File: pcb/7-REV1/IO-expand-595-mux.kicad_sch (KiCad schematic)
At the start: 58 parts, among them Q2 2N7002KT, U10 LM358_DFN, U11 LM358_DFN, U12 LM358_DFN, U13 LM358_DFN, U2 74LVC8T245BQ, U402 CD4067, U503 74HCT245BQ, U9 LM358_DFN

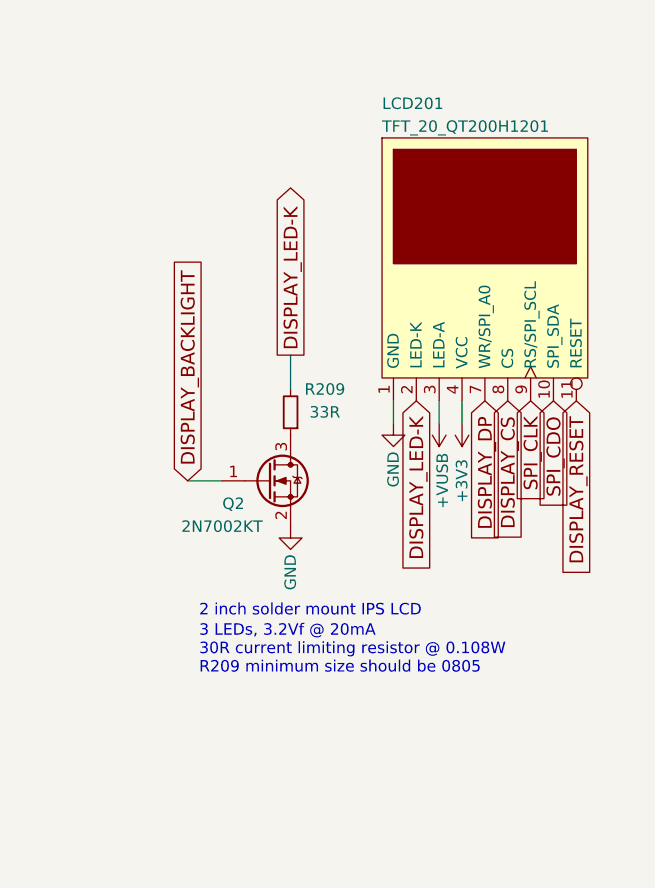
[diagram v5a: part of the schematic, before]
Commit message: move LCD background LED current limiting resistor from cathode to anode
- there were several soldering defects on the LCD connector observed during manufacturing
- often the LEDs were shorted to ground
- this modification will protect the LEDs and the traces in this case, making rework easier
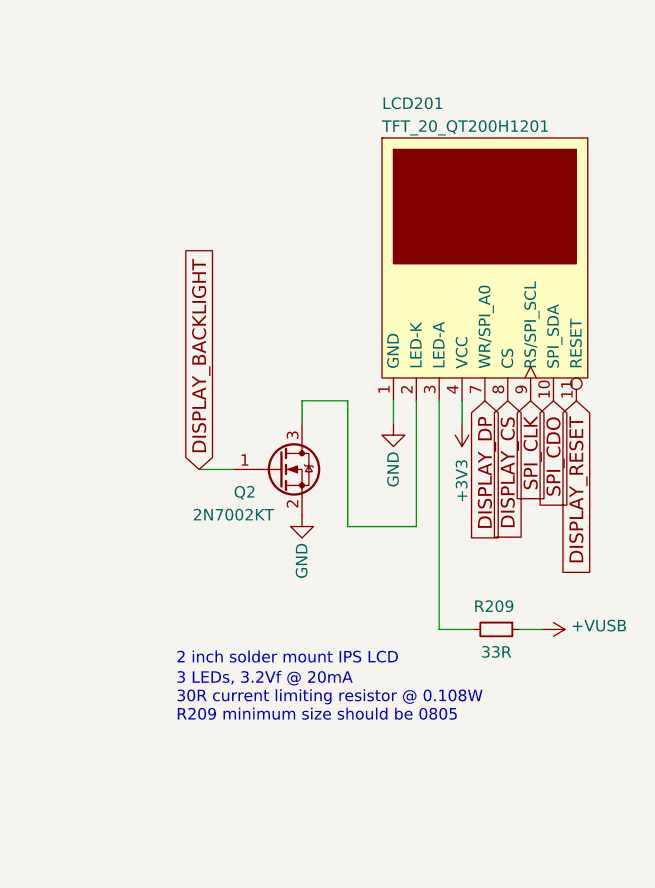
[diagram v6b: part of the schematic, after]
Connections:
- net +VUSB: now also R209.1; no longer LCD201.3 (LED-A)
- net at Q2.3 (D): now also LCD201.2 (LED-K); no longer R209.1
- net DISPLAY_LED-K: no longer names the net of R209.2
- net DISPLAY_LED-K: now also LCD201.3 (LED-A); no longer LCD201.2 (LED-K)
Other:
- moved on the sheet: Q2, R209
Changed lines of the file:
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@@
 	(wire
 		(pts
+			(xy 347.98 60.96) (xy 347.98 63.5)
+		)
+		(stroke
+			(width 0)
+			(type default)
+		)
+	)
+	(wire
+		(pts
 			(xy 157.48 121.92) (xy 157.48 115.57)
 		)
@@
 	(wire
 		(pts
+			(xy 360.68 60.96) (xy 360.68 74.93)
+		)
+		(stroke
+			(width 0)
+			(type default)
+		)
+	)
+	(wire
+		(pts
 			(xy 31.75 172.72) (xy 34.29 172.72)
 		)
@@
 	(wire
 		(pts
+			(xy 353.06 74.93) (xy 353.06 60.96)
+		)
+		(stroke
+			(width 0)
+			(type default)
+		)
+	)
+	(wire
+		(pts
 			(xy 240.03 139.7) (xy 237.49 139.7)
 		)
@@
 	(wire
 		(pts
+			(xy 372.11 86.36) (xy 374.65 86.36)
+		)
+		(stroke
+			(width 0)
+			(type default)
+		)
+	)
+	(wire
+		(pts
 			(xy 113.03 175.26) (xy 115.57 175.26)
 		)
@@
 	(wire
 		(pts
+			(xy 353.06 60.96) (xy 347.98 60.96)
+		)
+		(stroke
+			(width 0)
+			(type default)
+		)
+	)
+	(wire
+		(pts
 			(xy 260.35 125.73) (xy 260.35 128.27)
 		)
@@
 	(wire
 		(pts
+			(xy 360.68 74.93) (xy 353.06 74.93)
+		)
+		(stroke
+			(width 0)
+			(type default)
+		)
+	)
+	(wire
+		(pts
 			(xy 59.69 177.8) (xy 60.96 177.8)
 		)
@@
 	(wire
 		(pts
-			(xy 335.28 69.85) (xy 339.09 69.85)
+			(xy 336.55 68.58) (xy 340.36 68.58)
 		)
 		(stroke
@@
 	(wire
 		(pts
-			(xy 346.71 55.88) (xy 346.71 59.69)
-		)
-		(stroke
-			(width 0)
-			(type default)
-		)
-	)
-	(wire
-		(pts
 			(xy 48.26 223.52) (xy 50.8 223.52)
 		)
@@
 	(wire
 		(pts
-			(xy 363.22 60.96) (xy 363.22 63.5)
+			(xy 363.22 60.96) (xy 363.22 86.36)
 		)
 		(stroke
@@
 	(wire
 		(pts
+			(xy 367.03 86.36) (xy 363.22 86.36)
+		)
+		(stroke
+			(width 0)
+			(type default)
+		)
+	)
+	(wire
+		(pts
 			(xy 46.99 101.6) (xy 46.99 102.87)
 		)
@@
 	(text "3 LEDs, 3.2Vf @ 20mA\n30R current limiting resistor @ 0.108W\nR209 minimum size should be 0805"
 		(exclude_from_sim no)
-		(at 336.55 91.44 0)
+		(at 334.01 96.774 0)
 		(effects
 			(font
@@
 	(text "2 inch solder mount IPS LCD"
 		(exclude_from_sim no)
-		(at 336.55 85.09 0)
+		(at 334.01 90.424 0)
 		(effects
 			(font
@@
 		)
 	)
-	(global_label "DISPLAY_LED-K"
-		(shape output)
-		(at 346.71 55.88 90)
-		(effects
-			(font
-				(size 1.524 1.524)
-			)
-			(justify left)
-		)
-		(property "Intersheetrefs" "${INTERSHEET_REFS}"
-			(at 346.71 55.88 0)
-			(effects
-				(font
-					(size 1.27 1.27)
-				)
-				(hide yes)
-			)
-		)
-	)
 	(global_label "MUX_BPIO5_TVS"
 		(shape input)
@@
 	(global_label "DISPLAY_BACKLIGHT"
 		(shape input)
-		(at 335.28 69.85 90)
+		(at 336.55 68.58 90)
 		(effects
 			(font
@@
 		)
 		(property "Intersheetrefs" "${INTERSHEET_REFS}"
-			(at 335.28 69.85 0)
+			(at 336.55 68.58 0)
 			(effects
 				(font
@@
 		)
 	)
-	(global_label "DISPLAY_LED-K"
-		(shape input)
-		(at 360.68 60.96 270)
-		(effects
-			(font
-				(size 1.524 1.524)
-			)
-			(justify right)
-		)
-		(property "Intersheetrefs" "${INTERSHEET_REFS}"
-			(at 360.68 60.96 0)
-			(effects
-				(font
-					(size 1.27 1.27)
-				)
-				(hide yes)
-			)
-		)
-	)
 	(global_label "AMUX_OUT"
 		(shape output)
@@
 	(symbol
 		(lib_id "Device:R_Small")
-		(at 346.71 62.23 180)
+		(at 369.57 86.36 270)
 		(unit 1)
 		(exclude_from_sim no)
@@
 		(dnp no)
 		(property "Reference" "R209"
-			(at 350.52 59.69 0)
+			(at 369.316 83.82 90)
 			(effects
 				(font
@@
 		)
 		(property "Value" "33R"
-			(at 350.52 62.23 0)
+			(at 369.57 88.9 90)
 			(effects
 				(font
@@
 		)
 		(property "Footprint" "Resistor_SMD:R_0805_2012Metric"
-			(at 346.71 62.23 0)
+			(at 369.57 86.36 0)
 			(effects
 				(font
@@
 		)
 		(property "Datasheet" "~"
-			(at 346.71 62.23 0)
+			(at 369.57 86.36 0)
 			(effects
 				(font
@@
 		)
 		(property "Description" ""
-			(at 346.71 62.23 0)
+			(at 369.57 86.36 0)
 			(effects
 				(font
@@
 		)
 		(property "RMB" "0.019315"
-			(at 346.71 62.23 0)
+			(at 369.57 86.36 0)
 			(effects
 				(font
@@
 		)
 		(property "Supplier" "https://item.szlcsc.com/139271.html"
-			(at 346.71 62.23 0)
+			(at 369.57 86.36 0)
 			(effects
 				(font
@@
 		)
 		(property "Description_1" ""
-			(at 346.71 62.23 0)
+			(at 369.57 86.36 0)
 			(effects
 				(font
@@
 		)
 		(property "MAXIMUM_PACKAGE_HEIGHT" ""
-			(at 346.71 62.23 0)
+			(at 369.57 86.36 0)
 			(effects
 				(font
@@
 		)
 		(property "PARTREV" ""
-			(at 346.71 62.23 0)
+			(at 369.57 86.36 0)
 			(effects
 				(font
@@
 		)
 		(property "STANDARD" ""
-			(at 346.71 62.23 0)
+			(at 369.57 86.36 0)
 			(effects
 				(font
@@
 	(symbol
 		(lib_id "power:GND")
-		(at 346.71 74.93 0)
+		(at 347.98 73.66 0)
 		(unit 1)
 		(exclude_from_sim no)
@@
 		(dnp no)
 		(property "Reference" "#PWR0211"
-			(at 346.71 81.28 0)
+			(at 347.98 80.01 0)
 			(effects
 				(font
@@
 		)
 		(property "Value" "GND"
-			(at 346.71 80.01 90)
+			(at 347.98 78.74 90)
 			(effects
 				(font
@@
 		)
 		(property "Footprint" ""
-			(at 346.71 74.93 0)
+			(at 347.98 73.66 0)
 			(effects
 				(font
@@
 		)
 		(property "Datasheet" ""
-			(at 346.71 74.93 0)
+			(at 347.98 73.66 0)
 			(effects
 				(font
@@
 		)
 		(property "Description" ""
-			(at 346.71 74.93 0)
+			(at 347.98 73.66 0)
 			(effects
 				(font
@@
 	(symbol
 		(lib_id "dp-power:+VUSB")
-		(at 363.22 63.5 180)
+		(at 374.65 86.36 270)
 		(unit 1)
 		(exclude_from_sim no)
@@
 		(dnp no)
 		(property "Reference" "#PWR0213"
-			(at 363.22 63.5 0)
+			(at 374.65 86.36 0)
 			(effects
 				(font
@@
 		)
 		(property "Value" "+VUSB"
-			(at 363.601 66.7258 90)
+			(at 377.8758 85.979 90)
 			(effects
 				(font
@@
 		)
 		(property "Footprint" ""
-			(at 363.22 63.5 0)
+			(at 374.65 86.36 0)
 			(effects
 				(font
@@
 		)
 		(property "Datasheet" ""
-			(at 363.22 63.5 0)
+			(at 374.65 86.36 0)
 			(effects
 				(font
@@
 		)
 		(property "Description" ""
-			(at 363.22 63.5 0)
+			(at 374.65 86.36 0)
 			(effects
 				(font
@@
 	(symbol
 		(lib_id "Transistor_FET:BSS138")
-		(at 344.17 69.85 0)
+		(at 345.44 68.58 0)
 		(unit 1)
 		(exclude_from_sim no)
@@
 		(dnp no)
 		(property "Reference" "Q2"
-			(at 340.36 72.39 0)
+			(at 341.63 71.12 0)
 			(effects
 				(font
@@
 		)
 		(property "Value" "2N7002KT"
-			(at 339.09 74.93 0)
+			(at 340.36 73.66 0)
 			(effects
 				(font
@@
 		)
 		(property "Footprint" "Package_TO_SOT_SMD:SOT-523"
-			(at 349.25 71.755 0)
+			(at 350.52 70.485 0)
 			(effects
 				(font
@@
 		)
 		(property "Datasheet" "https://www.onsemi.com/download/data-sheet/pdf/2n7002t-d.pdf"
-			(at 344.17 69.85 0)
+			(at 345.44 68.58 0)
 			(effects
 				(font
@@
 		)
 		(property "Description" ""
-			(at 344.17 69.85 0)
+			(at 345.44 68.58 0)
 			(effects
 				(font
@@
 		)
 		(property "RMB" "0.140017"
-			(at 344.17 69.85 0)
+			(at 345.44 68.58 0)
 			(effects
 				(font
@@
 		)
 		(property "Supplier" "https://item.szlcsc.com/544697.html"
-			(at 344.17 69.85 0)
+			(at 345.44 68.58 0)
 			(effects
 				(font
@@
 		)
 		(property "Description_1" ""
-			(at 344.17 69.85 0)
+			(at 345.44 68.58 0)
 			(effects
 				(font
@@
 		)
 		(property "MANUFACTURER" "CBI"
-			(at 344.17 69.85 0)
+			(at 345.44 68.58 0)
 			(effects
 				(font
@@
 		)
 		(property "MAXIMUM_PACKAGE_HEIGHT" ""
-			(at 344.17 69.85 0)
+			(at 345.44 68.58 0)
 			(effects
 				(font
@@
 		)
 		(property "PARTREV" ""
-			(at 344.17 69.85 0)
+			(at 345.44 68.58 0)
 			(effects
 				(font
@@
 		)
 		(property "STANDARD" ""
-			(at 344.17 69.85 0)
+			(at 345.44 68.58 0)
 			(effects
 				(font
